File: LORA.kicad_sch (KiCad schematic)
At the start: 4 parts, among them J4 Conn_Coaxial, U4 HT-RA62

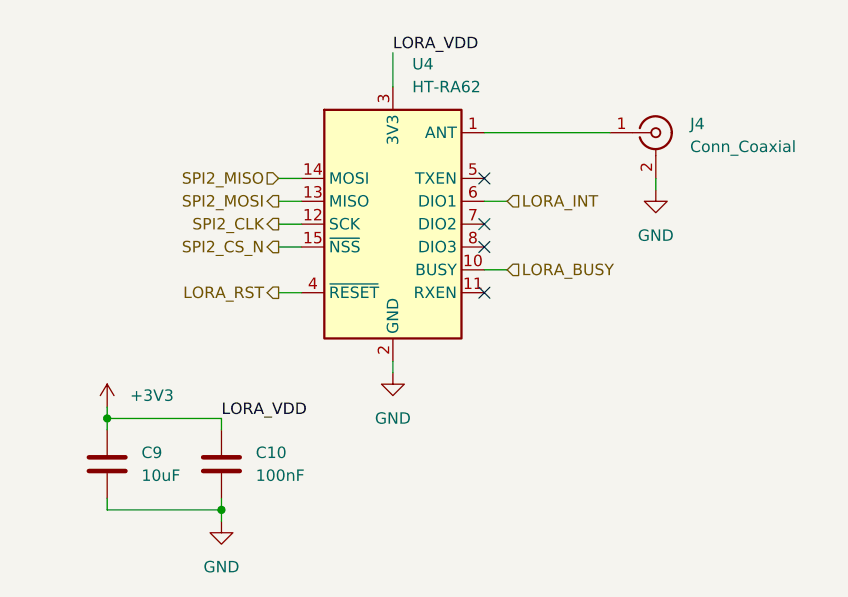
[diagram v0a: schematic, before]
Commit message: Round board corners, re-annotate test points, rewrite README for GitHub
Board: 1.0 mm radius corners; outline now 71.00 x 46.00 mm.
Schematic: test points re-annotated to signal names (SDA1, SLC1,
CSN1, CLK1, MOSI1, MISO1, VS1, G1, G2, IO7, IO15, IO47, RST1, BOOT1).

README rewritten as a GitHub landing page: explains what the board is
for, adds Mermaid system-architecture and power-path diagrams, a
verified pin map traced from the netlist, board specs, and fab
instructions. Drops the ERC/DRC status and issue-tracking sections.

Co-Authored-By: Claude Opus 5 <noreply@anthropic.com>
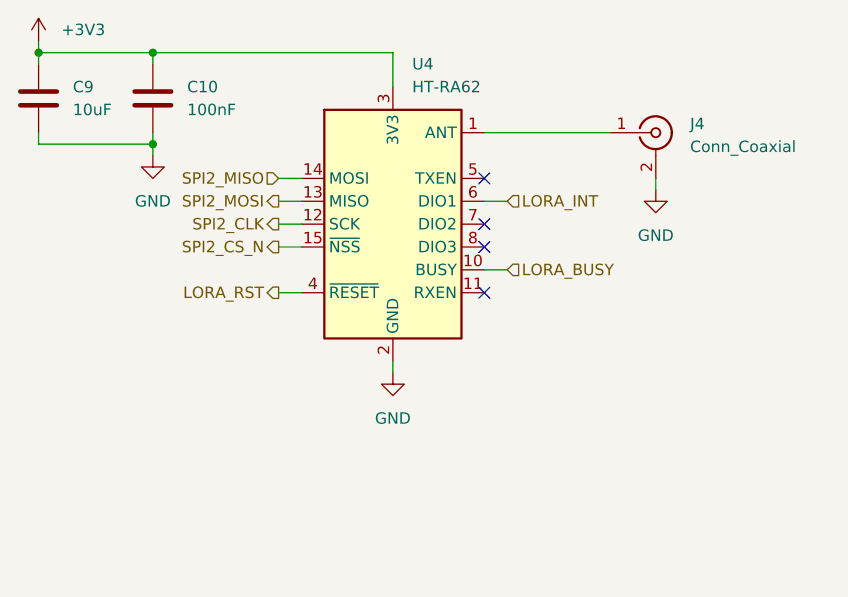
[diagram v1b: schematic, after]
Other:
- moved on the sheet: C10, C9
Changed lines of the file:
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@@
 	(paper "A4")
 	(junction
-		(at 101.6 95.25)
+		(at 93.98 54.61)
 		(diameter 0)
 		(color 0 0 0 0)
 	)
 	(junction
-		(at 114.3 105.41)
+		(at 106.68 54.61)
 		(diameter 0)
 		(color 0 0 0 0)
 	)
+	(junction
+		(at 106.68 64.77)
+		(diameter 0)
+		(color 0 0 0 0)
+	)
 	(no_connect
 		(at 143.51 68.58)
@@
 	(wire
 		(pts
-			(xy 101.6 96.52) (xy 101.6 95.25)
-		)
-		(stroke
-			(width 0)
-			(type default)
-		)
-	)
-	(wire
-		(pts
-			(xy 101.6 93.98) (xy 101.6 95.25)
+			(xy 93.98 55.88) (xy 93.98 54.61)
+		)
+		(stroke
+			(width 0)
+			(type default)
+		)
+	)
+	(wire
+		(pts
+			(xy 93.98 53.34) (xy 93.98 54.61)
 		)
 		(stroke
@@
 	(wire
 		(pts
-			(xy 101.6 105.41) (xy 101.6 104.14)
+			(xy 93.98 64.77) (xy 93.98 63.5)
 		)
 		(stroke
@@
 	(wire
 		(pts
+			(xy 106.68 54.61) (xy 133.35 54.61)
+		)
+		(stroke
+			(width 0)
+			(type default)
+		)
+	)
+	(wire
+		(pts
 			(xy 146.05 78.74) (xy 143.51 78.74)
 		)
@@
 	(wire
 		(pts
-			(xy 114.3 104.14) (xy 114.3 105.41)
-		)
-		(stroke
-			(width 0)
-			(type default)
-		)
-	)
-	(wire
-		(pts
-			(xy 114.3 105.41) (xy 101.6 105.41)
+			(xy 106.68 63.5) (xy 106.68 64.77)
+		)
+		(stroke
+			(width 0)
+			(type default)
+		)
+	)
+	(wire
+		(pts
+			(xy 106.68 64.77) (xy 93.98 64.77)
 		)
 		(stroke
@@
 	(wire
 		(pts
-			(xy 114.3 106.68) (xy 114.3 105.41)
+			(xy 106.68 66.04) (xy 106.68 64.77)
 		)
 		(stroke
@@
 	(wire
 		(pts
-			(xy 114.3 95.25) (xy 114.3 96.52)
+			(xy 106.68 54.61) (xy 106.68 55.88)
 		)
 		(stroke
@@
 	(wire
 		(pts
-			(xy 101.6 95.25) (xy 114.3 95.25)
+			(xy 93.98 54.61) (xy 106.68 54.61)
 		)
 		(stroke
@@
 			(width 0)
 			(type default)
-		)
-	)
-	(label "LORA_VDD"
-		(at 114.3 95.25 0)
-		(effects
-			(font
-				(size 1.27 1.27)
-			)
-			(justify left bottom)
-		)
-	)
-	(label "LORA_VDD"
-		(at 133.35 54.61 0)
-		(effects
-			(font
-				(size 1.27 1.27)
-			)
-			(justify left bottom)
 		)
 	)
@@
 	(symbol
 		(lib_id "power:GND")
-		(at 114.3 106.68 0)
+		(at 106.68 66.04 0)
 		(unit 1)
 		(body_style 1)
@@
 		(fields_autoplaced yes)
 		(property "Reference" "#PWR06"
-			(at 114.3 113.03 0)
+			(at 106.68 72.39 0)
 			(hide yes)
 			(show_name no)
@@
 		)
 		(property "Value" "GND"
-			(at 114.3 111.76 0)
+			(at 106.68 71.12 0)
 			(show_name no)
 			(do_not_autoplace no)
@@
 		)
 		(property "Footprint" ""
-			(at 114.3 106.68 0)
+			(at 106.68 66.04 0)
 			(hide yes)
 			(show_name no)
@@
 		)
 		(property "Datasheet" ""
-			(at 114.3 106.68 0)
+			(at 106.68 66.04 0)
 			(hide yes)
 			(show_name no)
@@
 		)
 		(property "Description" "Power symbol creates a global label with name \"GND\" , ground"
-			(at 114.3 106.68 0)
+			(at 106.68 66.04 0)
 			(hide yes)
 			(show_name no)
@@
 	(symbol
 		(lib_id "Device:C")
-		(at 101.6 100.33 0)
+		(at 93.98 59.69 0)
 		(unit 1)
 		(body_style 1)
@@
 		(fields_autoplaced yes)
 		(property "Reference" "C9"
-			(at 105.41 99.0599 0)
+			(at 97.79 58.4199 0)
 			(show_name no)
 			(do_not_autoplace no)
@@
 		)
 		(property "Value" "10uF"
-			(at 105.41 101.5999 0)
+			(at 97.79 60.9599 0)
 			(show_name no)
 			(do_not_autoplace no)
@@
 		)
 		(property "Footprint" "Capacitor_SMD:C_0805_2012Metric_Pad1.18x1.45mm_HandSolder"
-			(at 102.5652 104.14 0)
+			(at 94.9452 63.5 0)
 			(hide yes)
 			(show_name no)
@@
 		)
 		(property "Datasheet" ""
-			(at 101.6 100.33 0)
+			(at 93.98 59.69 0)
 			(hide yes)
 			(show_name no)
@@
 		)
 		(property "Description" "Unpolarized capacitor"
-			(at 101.6 100.33 0)
+			(at 93.98 59.69 0)
 			(hide yes)
 			(show_name no)
@@
 	(symbol
 		(lib_id "power:+3V3")
-		(at 101.6 93.98 0)
+		(at 93.98 53.34 0)
 		(unit 1)
 		(body_style 1)
@@
 		(fields_autoplaced yes)
 		(property "Reference" "#PWR031"
-			(at 101.6 97.79 0)
+			(at 93.98 57.15 0)
 			(hide yes)
 			(show_name no)
@@
 		)
 		(property "Value" "+3V3"
-			(at 104.14 92.7099 0)
+			(at 96.52 52.0699 0)
 			(show_name no)
 			(do_not_autoplace no)
@@
 		)
 		(property "Footprint" ""
-			(at 101.6 93.98 0)
+			(at 93.98 53.34 0)
 			(hide yes)
 			(show_name no)
@@
 		)
 		(property "Datasheet" ""
-			(at 101.6 93.98 0)
+			(at 93.98 53.34 0)
 			(hide yes)
 			(show_name no)
@@
 		)
 		(property "Description" "Power symbol creates a global label with name \"+3V3\""
-			(at 101.6 93.98 0)
+			(at 93.98 53.34 0)
 			(hide yes)
 			(show_name no)
@@
 	(symbol
 		(lib_id "Device:C")
-		(at 114.3 100.33 0)
+		(at 106.68 59.69 0)
 		(unit 1)
 		(body_style 1)
@@
 		(fields_autoplaced yes)
 		(property "Reference" "C10"
-			(at 118.11 99.0599 0)
+			(at 110.49 58.4199 0)
 			(show_name no)
 			(do_not_autoplace no)
@@
 		)
 		(property "Value" "100nF"
-			(at 118.11 101.5999 0)
+			(at 110.49 60.9599 0)
 			(show_name no)
 			(do_not_autoplace no)
@@
 		)
 		(property "Footprint" "Capacitor_SMD:C_0805_2012Metric_Pad1.18x1.45mm_HandSolder"
-			(at 115.2652 104.14 0)
+			(at 107.6452 63.5 0)
 			(hide yes)
 			(show_name no)
@@
 		)
 		(property "Datasheet" ""
-			(at 114.3 100.33 0)
+			(at 106.68 59.69 0)
 			(hide yes)
 			(show_name no)
@@
 		)
 		(property "Description" "Unpolarized capacitor"
-			(at 114.3 100.33 0)
-			(hide yes)
-			(show_name no)
+			(at 106.68 59.69 0)
+			(hide yes)
+			(show_name no)
